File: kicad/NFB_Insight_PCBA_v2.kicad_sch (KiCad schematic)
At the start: 0 parts

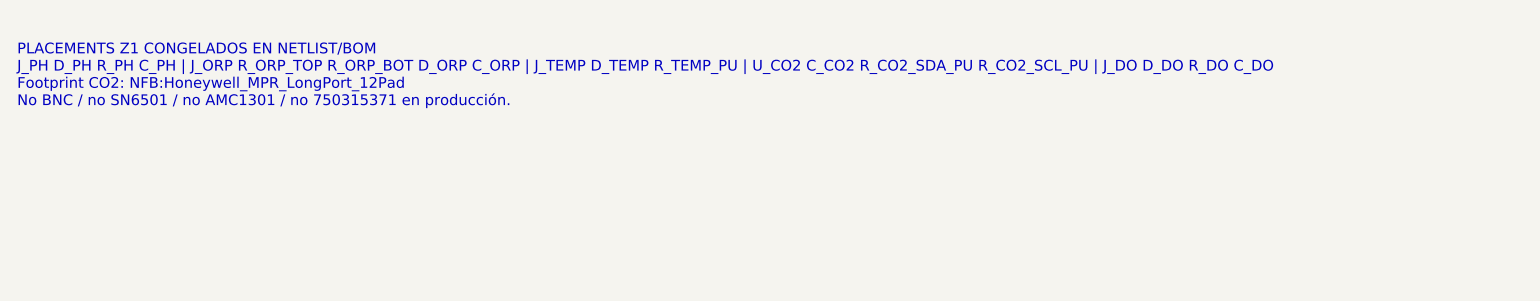
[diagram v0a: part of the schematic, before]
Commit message: fix(ci): documentar referencias Z1 en hoja contractual
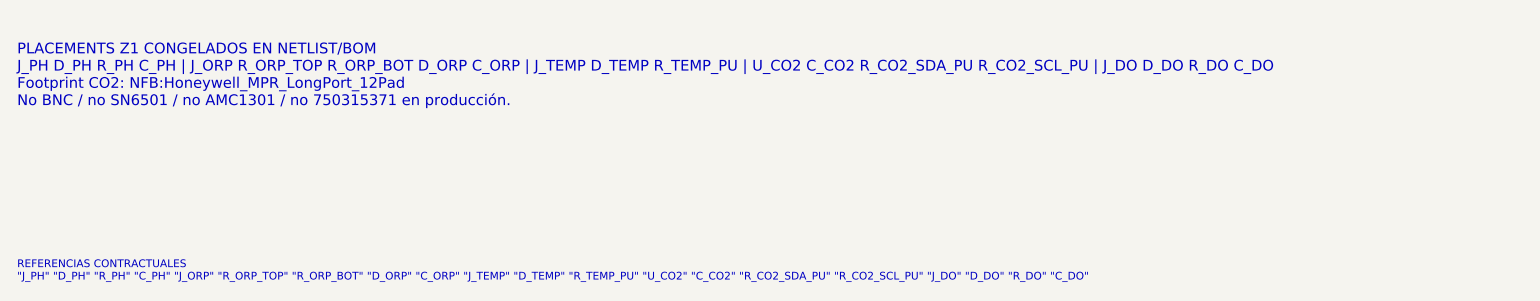
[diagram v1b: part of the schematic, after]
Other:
- note added: "REFERENCIAS CONTRACTUALES "J_PH" "D_PH" "R_PH" "C_PH" "J_ORP" "R_ORP_TOP" "R_ORP_BOT" "D_ORP" "C_ORP" "J_TEMP" "D_TEMP" "R_TEMP_PU" "U_CO2" "C_CO2" "R_CO2_SDA_PU" "R_CO2_SCL_PU" "J_DO" "D_DO" "R_DO" "C_DO""
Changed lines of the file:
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@@
     (title "NFB Insight PCBA v2 — Z1 Sensor Production Contract")
     (date "2026-08-11")
-    (rev "0.6.3")
+    (rev "0.6.4")
     (company "Cafelium SRL / Nebula Ecosystem")
     (comment 1 "PR #6 — contrato discreto Z1 gobernado por hardware/z1_production_netlist.json")
@@
     (effects (font (size 1.25 1.25)) (justify left bottom))
   )
+  (text "REFERENCIAS CONTRACTUALES\n\"J_PH\" \"D_PH\" \"R_PH\" \"C_PH\" \"J_ORP\" \"R_ORP_TOP\" \"R_ORP_BOT\" \"D_ORP\" \"C_ORP\" \"J_TEMP\" \"D_TEMP\" \"R_TEMP_PU\" \"U_CO2\" \"C_CO2\" \"R_CO2_SDA_PU\" \"R_CO2_SCL_PU\" \"J_DO\" \"D_DO\" \"R_DO\" \"C_DO\""
+    (exclude_from_sim no)
+    (at 38.1 294.64 0)
+    (effects (font (size 0.9 0.9)) (justify left bottom))
+  )
   (sheet_instances

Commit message: fix(ci): indexar referencias contractuales Z1
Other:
- note added: "C_CO2"
- note added: "C_DO"
- note added: "C_ORP"
- note added: "C_PH"
- note added: "D_DO"
- note added: "D_ORP"
- note added: "D_PH"
- note added: "D_TEMP"
- note added: "J_DO"
- note added: "J_ORP"
- note added: "J_PH"
- note added: "J_TEMP"
- note added: "R_CO2_SCL_PU"
- note added: "R_CO2_SDA_PU"
- note added: "R_DO"
- note added: "R_ORP_BOT"
- note added: "R_ORP_TOP"
- note added: "R_PH"
- note added: "R_TEMP_PU"
- note added: "U_CO2"
- note removed: "REFERENCIAS CONTRACTUALES "J_PH" "D_PH" "R_PH" "C_PH" "J_ORP" "R_ORP_TOP" "R_ORP_BOT" "D_ORP" "C_ORP" "J_TEMP" "D_TEMP" "R_TEMP_PU" "U_CO2" "C_CO2" "R_CO2_SDA_PU" "R_CO2_SCL_PU" "J_DO" "D_DO" "R_DO" "C_DO""
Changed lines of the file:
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@@
   (version 20250114)
   (generator "nfb_pr6_contract")
-  (generator_version "1.3")
+  (generator_version "1.4")
   (paper "A3")
   (title_block
     (title "NFB Insight PCBA v2 — Z1 Sensor Production Contract")
     (date "2026-08-11")
-    (rev "0.6.4")
+    (rev "0.6.5")
     (company "Cafelium SRL / Nebula Ecosystem")
     (comment 1 "PR #6 — contrato discreto Z1 gobernado por hardware/z1_production_netlist.json")
@@
     (effects (font (size 1.25 1.25)) (justify left bottom))
   )
-  (text "REFERENCIAS CONTRACTUALES\n\"J_PH\" \"D_PH\" \"R_PH\" \"C_PH\" \"J_ORP\" \"R_ORP_TOP\" \"R_ORP_BOT\" \"D_ORP\" \"C_ORP\" \"J_TEMP\" \"D_TEMP\" \"R_TEMP_PU\" \"U_CO2\" \"C_CO2\" \"R_CO2_SDA_PU\" \"R_CO2_SCL_PU\" \"J_DO\" \"D_DO\" \"R_DO\" \"C_DO\""
-    (exclude_from_sim no)
-    (at 38.1 294.64 0)
-    (effects (font (size 0.9 0.9)) (justify left bottom))
-  )
+  (text "J_PH" (exclude_from_sim no) (at 38.1 310 0) (effects (font (size 0.5 0.5)) (justify left bottom)))
+  (text "D_PH" (exclude_from_sim no) (at 90 310 0) (effects (font (size 0.5 0.5)) (justify left bottom)))
+  (text "R_PH" (exclude_from_sim no) (at 142 310 0) (effects (font (size 0.5 0.5)) (justify left bottom)))
+  (text "C_PH" (exclude_from_sim no) (at 194 310 0) (effects (font (size 0.5 0.5)) (justify left bottom)))
+  (text "J_ORP" (exclude_from_sim no) (at 38.1 315.08 0) (effects (font (size 0.5 0.5)) (justify left bottom)))
+  (text "R_ORP_TOP" (exclude_from_sim no) (at 90 315.08 0) (effects (font (size 0.5 0.5)) (justify left bottom)))
+  (text "R_ORP_BOT" (exclude_from_sim no) (at 142 315.08 0) (effects (font (size 0.5 0.5)) (justify left bottom)))
+  (text "D_ORP" (exclude_from_sim no) (at 194 315.08 0) (effects (font (size 0.5 0.5)) (justify left bottom)))
+  (text "C_ORP" (exclude_from_sim no) (at 38.1 320.16 0) (effects (font (size 0.5 0.5)) (justify left bottom)))
+  (text "J_TEMP" (exclude_from_sim no) (at 90 320.16 0) (effects (font (size 0.5 0.5)) (justify left bottom)))
+  (text "D_TEMP" (exclude_from_sim no) (at 142 320.16 0) (effects (font (size 0.5 0.5)) (justify left bottom)))
+  (text "R_TEMP_PU" (exclude_from_sim no) (at 194 320.16 0) (effects (font (size 0.5 0.5)) (justify left bottom)))
+  (text "U_CO2" (exclude_from_sim no) (at 38.1 325.24 0) (effects (font (size 0.5 0.5)) (justify left bottom)))
+  (text "C_CO2" (exclude_from_sim no) (at 90 325.24 0) (effects (font (size 0.5 0.5)) (justify left bottom)))
+  (text "R_CO2_SDA_PU" (exclude_from_sim no) (at 142 325.24 0) (effects (font (size 0.5 0.5)) (justify left bottom)))
+  (text "R_CO2_SCL_PU" (exclude_from_sim no) (at 194 325.24 0) (effects (font (size 0.5 0.5)) (justify left bottom)))
+  (text "J_DO" (exclude_from_sim no) (at 38.1 330.32 0) (effects (font (size 0.5 0.5)) (justify left bottom)))
+  (text "D_DO" (exclude_from_sim no) (at 90 330.32 0) (effects (font (size 0.5 0.5)) (justify left bottom)))
+  (text "R_DO" (exclude_from_sim no) (at 142 330.32 0) (effects (font (size 0.5 0.5)) (justify left bottom)))
+  (text "C_DO" (exclude_from_sim no) (at 194 330.32 0) (effects (font (size 0.5 0.5)) (justify left bottom)))
   (sheet_instances
     (path "/" (page "1"))

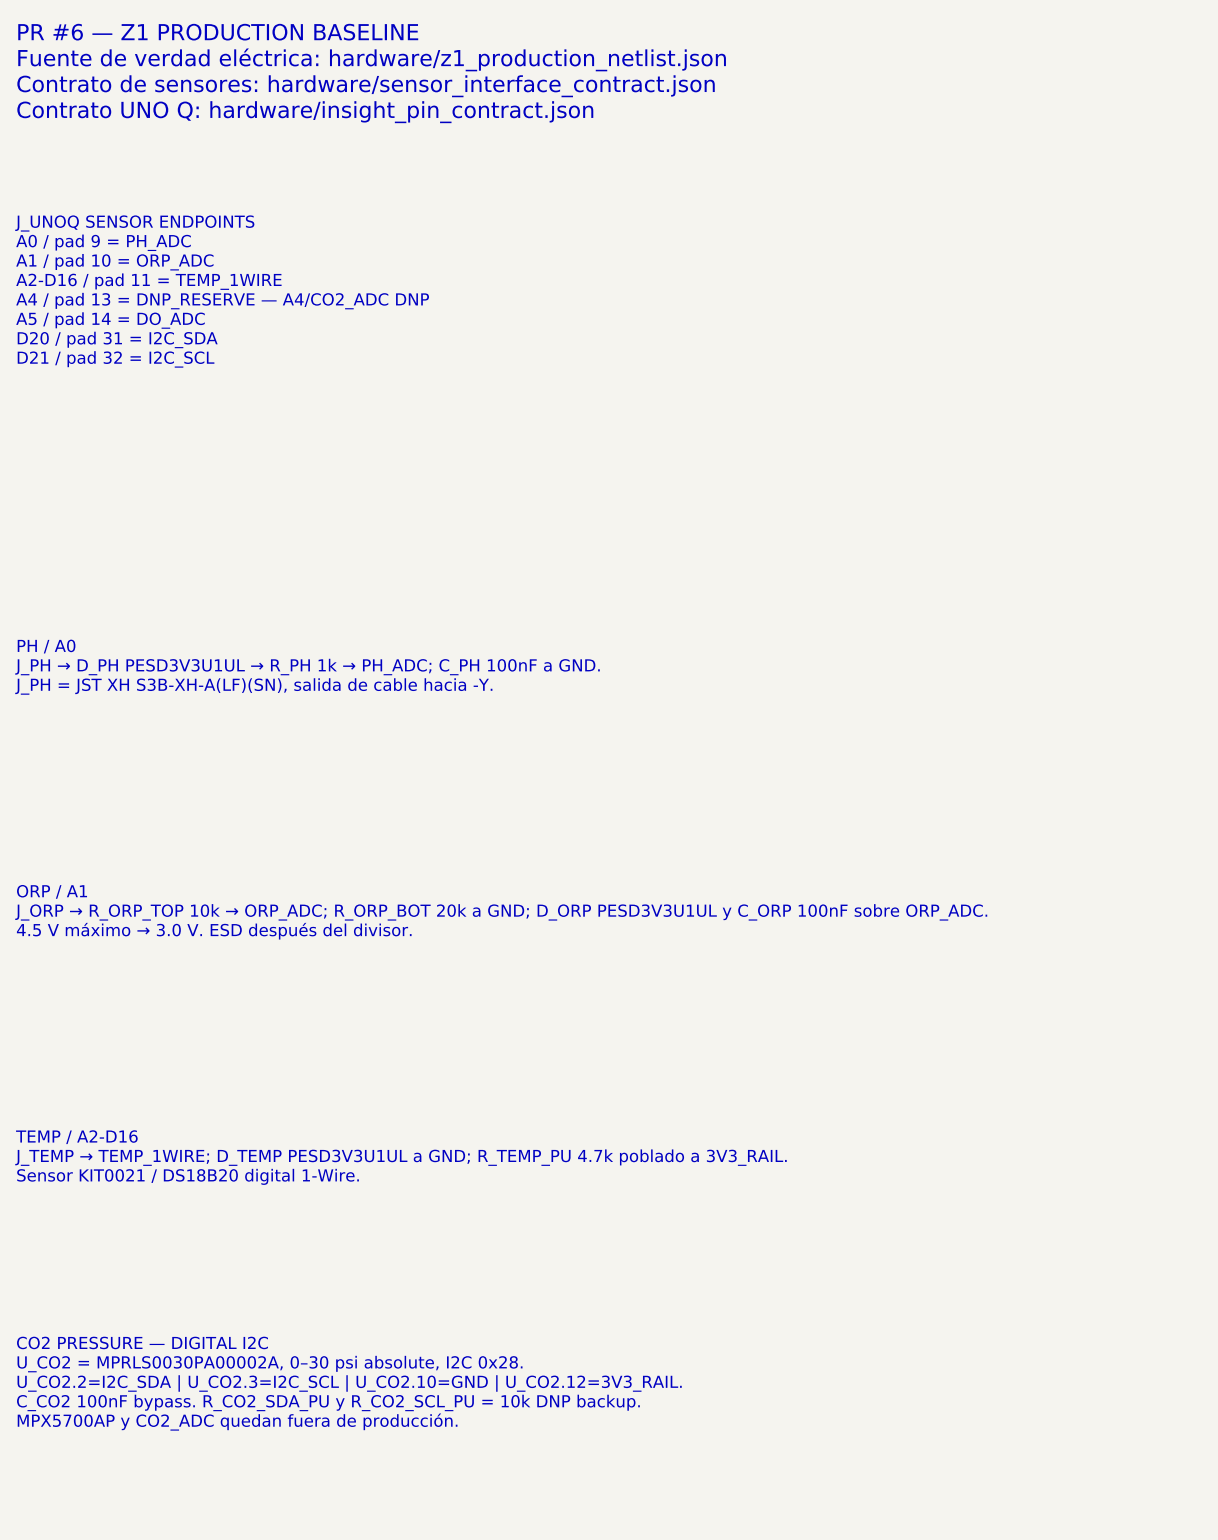
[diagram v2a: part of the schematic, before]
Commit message: kicad: anotar rails locales Z1 tras PR9
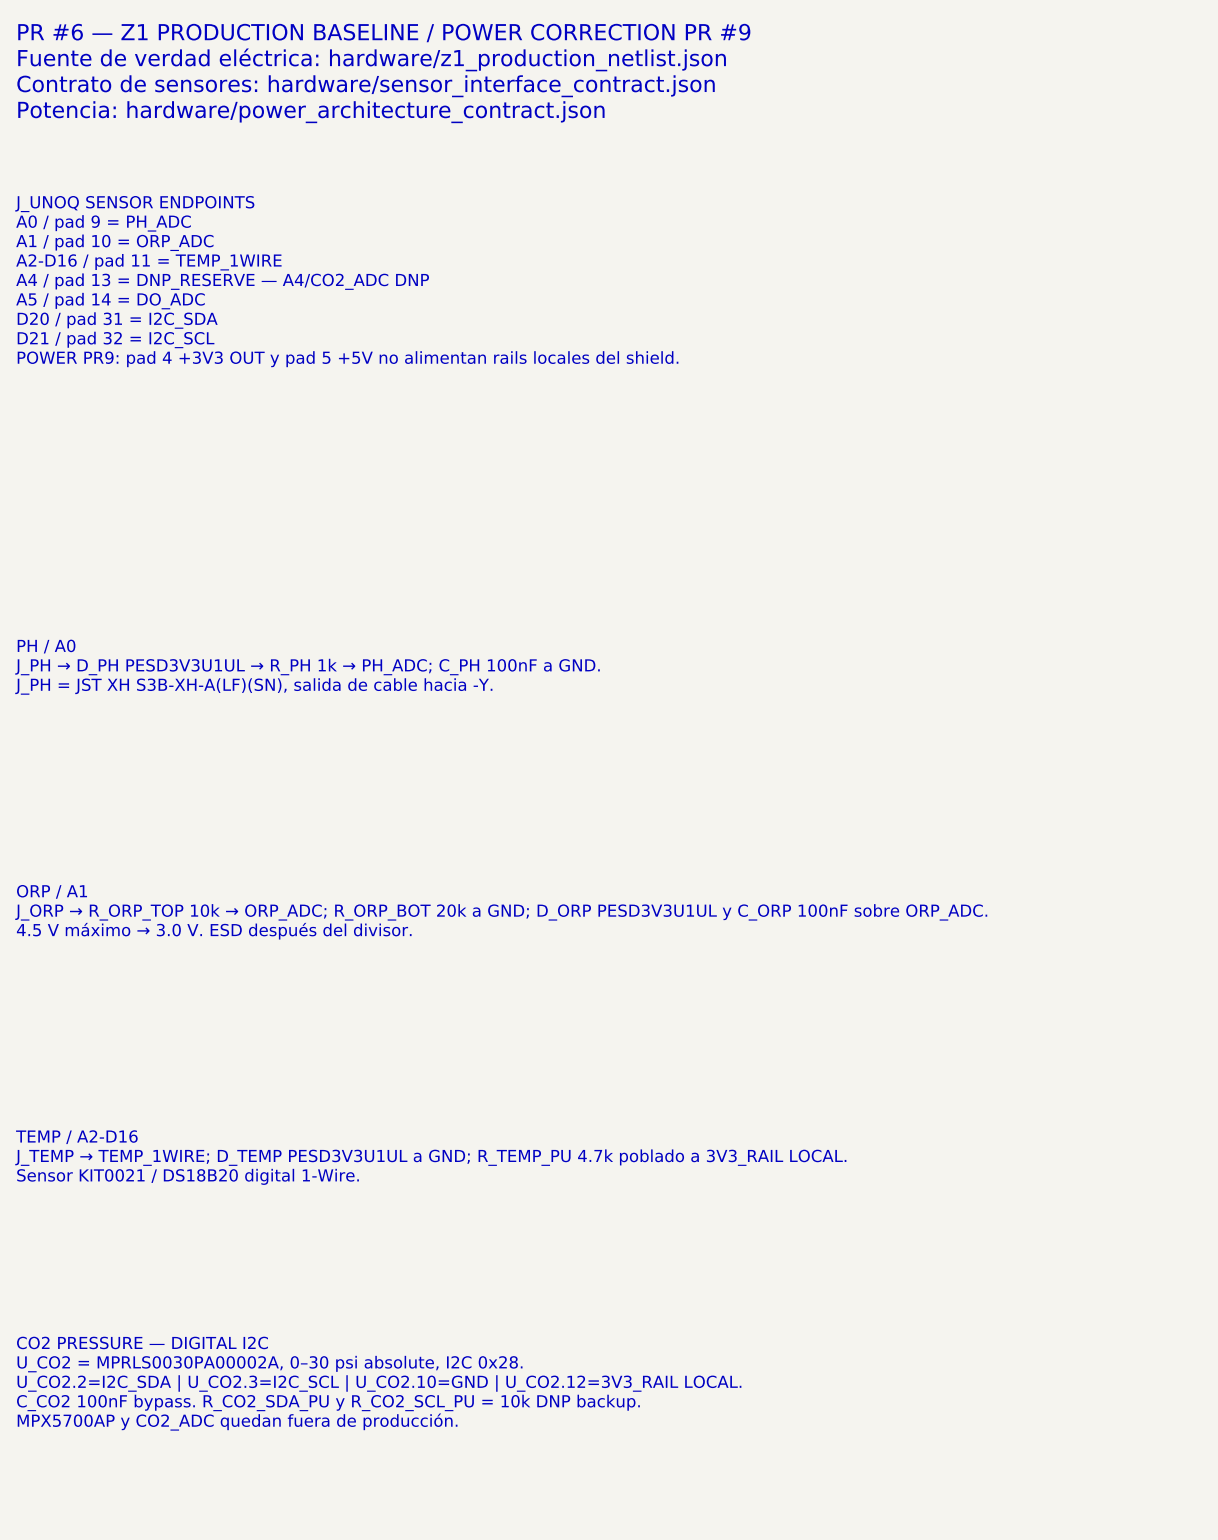
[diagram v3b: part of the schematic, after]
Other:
- note added: "CO2 PRESSURE — DIGITAL I2C U_CO2 = MPRLS0030PA00002A, 0–30 psi absolute, I2C 0x28. U_CO2.2=I2C_SDA | U_CO2.3=I2C_SCL | U_CO2.10=GND | U_CO2.12=3V3_RAIL LOCAL. C_CO2 100nF bypass. R_CO2_SDA_PU y R_CO2_SCL_PU = 10k DNP backup. MPX5700AP y CO2_ADC quedan fuera de producción."
- note added: "J_UNOQ SENSOR ENDPOINTS A0 / pad 9 = PH_ADC A1 / pad 10 = ORP_ADC A2-D16 / pad 11 = TEMP_1WIRE A4 / pad 13 = DNP_RESERVE — A4/CO2_ADC DNP A5 / pad 14 = DO_ADC D20 / pad 31 = I2C_SDA D21 / pad 32 = I2C_SCL POWER PR9: pad 4 +3V3 OUT y pad 5 +5V no alimentan rails locales del shield."
- note added: "PR #6 — Z1 PRODUCTION BASELINE / POWER CORRECTION PR #9 Fuente de verdad eléctrica: hardware/z1_production_netlist.json Contrato de sensores: hardware/sensor_interface_contract.json Potencia: hardware/power_architecture_contract.json"
- note added: "TEMP / A2-D16 J_TEMP → TEMP_1WIRE; D_TEMP PESD3V3U1UL a GND; R_TEMP_PU 4.7k poblado a 3V3_RAIL LOCAL. Sensor KIT0021 / DS18B20 digital 1-Wire."
- note removed: "CO2 PRESSURE — DIGITAL I2C U_CO2 = MPRLS0030PA00002A, 0–30 psi absolute, I2C 0x28. U_CO2.2=I2C_SDA | U_CO2.3=I2C_SCL | U_CO2.10=GND | U_CO2.12=3V3_RAIL. C_CO2 100nF bypass. R_CO2_SDA_PU y R_CO2_SCL_PU = 10k DNP backup. MPX5700AP y CO2_ADC quedan fuera de producción."
- note removed: "J_UNOQ SENSOR ENDPOINTS A0 / pad 9 = PH_ADC A1 / pad 10 = ORP_ADC A2-D16 / pad 11 = TEMP_1WIRE A4 / pad 13 = DNP_RESERVE — A4/CO2_ADC DNP A5 / pad 14 = DO_ADC D20 / pad 31 = I2C_SDA D21 / pad 32 = I2C_SCL"
- note removed: "PR #6 — Z1 PRODUCTION BASELINE Fuente de verdad eléctrica: hardware/z1_production_netlist.json Contrato de sensores: hardware/sensor_interface_contract.json Contrato UNO Q: hardware/insight_pin_contract.json"
- note removed: "TEMP / A2-D16 J_TEMP → TEMP_1WIRE; D_TEMP PESD3V3U1UL a GND; R_TEMP_PU 4.7k poblado a 3V3_RAIL. Sensor KIT0021 / DS18B20 digital 1-Wire."
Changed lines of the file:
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@@
   (version 20250114)
   (generator "nfb_pr6_contract")
-  (generator_version "1.4")
+  (generator_version "1.5")
   (paper "A3")
   (title_block
     (title "NFB Insight PCBA v2 — Z1 Sensor Production Contract")
     (date "2026-08-11")
-    (rev "0.6.5")
+    (rev "0.9.0")
     (company "Cafelium SRL / Nebula Ecosystem")
-    (comment 1 "PR #6 — contrato discreto Z1 gobernado por hardware/z1_production_netlist.json")
+    (comment 1 "PR #6 Z1 preservado; frontera de potencia corregida por PR #9")
     (comment 2 "BOM: bom/insight_z1_production_bom.csv")
     (comment 3 "A4/CO2_ADC DNP; CO2=MPRLS0030PA00002A I2C 0x28")
-    (comment 4 "Hoja raíz contractual; placement/routing fuera de alcance")
+    (comment 4 "5V_RAIL/3V3_RAIL son locales al shield; J_UNOQ.4/.5 no los alimentan")
   )
-  (text "PR #6 — Z1 PRODUCTION BASELINE\nFuente de verdad eléctrica: hardware/z1_production_netlist.json\nContrato de sensores: hardware/sensor_interface_contract.json\nContrato UNO Q: hardware/insight_pin_contract.json"
+  (text "PR #6 — Z1 PRODUCTION BASELINE / POWER CORRECTION PR #9\nFuente de verdad eléctrica: hardware/z1_production_netlist.json\nContrato de sensores: hardware/sensor_interface_contract.json\nPotencia: hardware/power_architecture_contract.json"
     (exclude_from_sim no)
     (at 38.1 35.56 0)
     (effects (font (size 2.0 2.0)) (justify left bottom))
   )
-  (text "J_UNOQ SENSOR ENDPOINTS\nA0 / pad 9 = PH_ADC\nA1 / pad 10 = ORP_ADC\nA2-D16 / pad 11 = TEMP_1WIRE\nA4 / pad 13 = DNP_RESERVE — A4/CO2_ADC DNP\nA5 / pad 14 = DO_ADC\nD20 / pad 31 = I2C_SDA\nD21 / pad 32 = I2C_SCL"
+  (text "J_UNOQ SENSOR ENDPOINTS\nA0 / pad 9 = PH_ADC\nA1 / pad 10 = ORP_ADC\nA2-D16 / pad 11 = TEMP_1WIRE\nA4 / pad 13 = DNP_RESERVE — A4/CO2_ADC DNP\nA5 / pad 14 = DO_ADC\nD20 / pad 31 = I2C_SDA\nD21 / pad 32 = I2C_SCL\nPOWER PR9: pad 4 +3V3 OUT y pad 5 +5V no alimentan rails locales del shield."
     (exclude_from_sim no)
     (at 38.1 66.04 0)
@@
     (effects (font (size 1.5 1.5)) (justify left bottom))
   )
-  (text "TEMP / A2-D16\nJ_TEMP → TEMP_1WIRE; D_TEMP PESD3V3U1UL a GND; R_TEMP_PU 4.7k poblado a 3V3_RAIL.\nSensor KIT0021 / DS18B20 digital 1-Wire."
+  (text "TEMP / A2-D16\nJ_TEMP → TEMP_1WIRE; D_TEMP PESD3V3U1UL a GND; R_TEMP_PU 4.7k poblado a 3V3_RAIL LOCAL.\nSensor KIT0021 / DS18B20 digital 1-Wire."
     (exclude_from_sim no)
     (at 38.1 167.64 0)
     (effects (font (size 1.5 1.5)) (justify left bottom))
   )
-  (text "CO2 PRESSURE — DIGITAL I2C\nU_CO2 = MPRLS0030PA00002A, 0–30 psi absolute, I2C 0x28.\nU_CO2.2=I2C_SDA | U_CO2.3=I2C_SCL | U_CO2.10=GND | U_CO2.12=3V3_RAIL.\nC_CO2 100nF bypass. R_CO2_SDA_PU y R_CO2_SCL_PU = 10k DNP backup.\nMPX5700AP y CO2_ADC quedan fuera de producción."
+  (text "CO2 PRESSURE — DIGITAL I2C\nU_CO2 = MPRLS0030PA00002A, 0–30 psi absolute, I2C 0x28.\nU_CO2.2=I2C_SDA | U_CO2.3=I2C_SCL | U_CO2.10=GND | U_CO2.12=3V3_RAIL LOCAL.\nC_CO2 100nF bypass. R_CO2_SDA_PU y R_CO2_SCL_PU = 10k DNP backup.\nMPX5700AP y CO2_ADC quedan fuera de producción."
     (exclude_from_sim no)
     (at 38.1 198.12 0)
